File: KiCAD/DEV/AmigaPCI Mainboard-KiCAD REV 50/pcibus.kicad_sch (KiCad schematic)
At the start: 61 parts, among them CN100 PCI32-5V, CN101 PCI32-5V, CN102 PCI32-5V, CN103 PCI32-5V, CN104 PCI32-5V, U814 74LVC245, U815 74LVC08, U816 74LVC245, U817 74LVC245

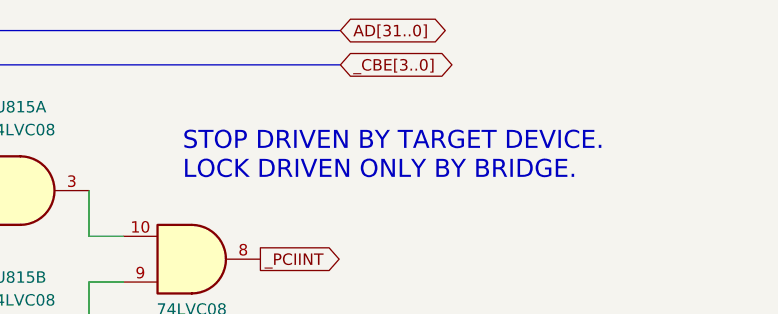
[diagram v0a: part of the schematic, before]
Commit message: Updated STM32F205 microcontroller.
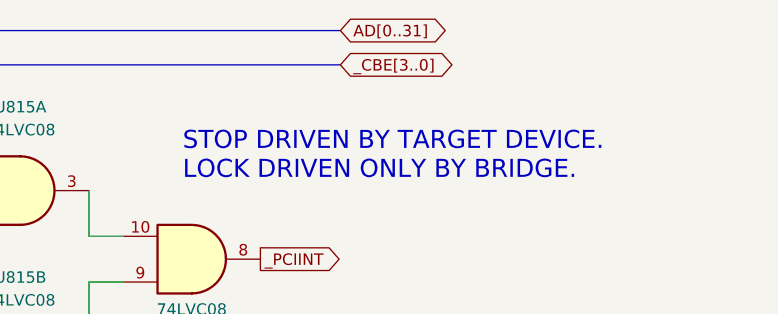
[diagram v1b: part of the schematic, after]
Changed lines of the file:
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@@
 		)
 	)
-	(global_label "AD[31..0]"
+	(global_label "AD[0..31]"
 		(shape bidirectional)
 		(at 378.46 17.78 0)

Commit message: Rev 5.0 APCI Update
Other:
- note added: "ADDRESS PHASE DATA PHASE ------------- ------------- PAR _PERR PAR _PERR --------------------------------------- CPU WR BRIDGE PCI BRIDGE PCI CPU RD BRIDGE PCI PCI BRIDGE DMA WR PCI BRIDGE PCI BRIDGE DMA RD PCI BRIDGE BRIDGE PCI"
- note removed: "-> DMA RD -> -> CPU WR -> <- DMA WR <- <- CPU RD <-"
- note removed: "TARGET INIT"
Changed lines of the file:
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@@
 	(title_block
 		(title "AMIGA PCI")
-		(date "2025-01-01")
+		(date "2025-01-10")
 		(rev "5.0")
 	)
@@
 		)
 	)
-	(text "-> DMA RD ->\n-> CPU WR ->\n\n<- DMA WR <-\n<- CPU RD <-\n"
-		(exclude_from_sim no)
-		(at 365.506 94.742 0)
-		(effects
-			(font
-				(size 1.27 1.27)
-			)
-		)
-	)
 	(text "DESIGNED TO COMPLY WITH \nPCI REV 2.3 SPECS.\n+5V SIGNALING ENVIRONMENT \nCOMPATABLE WITH UNIVERSAL CARDS."
 		(exclude_from_sim no)
@@
 		)
 	)
-	(text "TARGET       INIT"
+	(text "PULL ME!"
 		(exclude_from_sim no)
-		(at 347.98 65.278 0)
+		(at 350.52 229.87 0)
 		(effects
 			(font
-				(size 1.27 1.27)
+				(size 3 3)
 			)
+			(justify left bottom)
 		)
 	)
-	(text "PULL ME!"
+	(text "        ADDRESS PHASE     DATA PHASE\n        -------------     -------------\n        PAR     _PERR     PAR    _PERR\n---------------------------------------\nCPU WR  BRIDGE  PCI       BRIDGE PCI\nCPU RD  BRIDGE  PCI       PCI    BRIDGE\nDMA WR  PCI     BRIDGE    PCI    BRIDGE \nDMA RD  PCI     BRIDGE    BRIDGE PCI"
 		(exclude_from_sim no)
-		(at 350.52 229.87 0)
+		(at 371.094 81.28 0)
 		(effects
 			(font
-				(size 3 3)
+				(face "DejaVu Sans Mono")
+				(size 1.27 1.27)
 			)
-			(justify left bottom)
+			(justify left)
 		)
 	)
